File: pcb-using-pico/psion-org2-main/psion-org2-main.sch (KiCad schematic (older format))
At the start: 80 parts, among them J1 Conn_01x24_Female, J2 Conn_01x03_Female, J3 Conn_01x27_Female, J4 Conn_01x02_Female, J5 Conn_01x02_Female, J6 Conn_01x11_Female, M1 P-CH-MOSFET, M2 P-CHANNEL-MOSFET, M3 P-CHANNEL-MOSFET, U1 Pico, U10 AMS1117-3.3, U2 74HC595, U3 Regulator_Switching_MT3608, U4 74LS165, U5 74HC595, U7 MCP7940N-xSN, Y1 32k768Hz

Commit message: Updates
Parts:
- D3, D4, D5: value D -> 1N4148
- D8, D9: value D -> AECQ101
- M1: value P-CH-MOSFET -> Si2301
- M2, M3: value P-CHANNEL-MOSFET -> Si2301
- R10, R18, R24: value 110k -> 10k
- R12: value 4k7 -> 5789
- R13, R14, R15: value 100k -> 10k
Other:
- note added: "Battery measurement ciruit not tested yet\nValues unknown. Zener diode may be needed."
- note added: "JP1: leave open until output of U3 is confirmed\nat 12V."
- note added: "JP2:Leave open until ready to test the 12V\nsupply to the OLED display."
- note added: "JP4,JP6:Leave open until ready to power all of the regulators"
- note added: "Problem can occur with RTC where it holds the supply on.\nRemove R10 to disable RTC power up feature."
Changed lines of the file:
@@
 AR Path="/61545310" Ref="R12"  Part="1"
 F 0 "R12" H 10759 9621 50  0000 L CNN
-F 1 "4k7" H 10759 9530 50  0000 L CNN
+F 1 "5789" H 10759 9530 50  0000 L CNN
 F 2 "Resistor_SMD:R_0805_2012Metric" H 10700 9575 50  0001 C CNN
 F 3 "~" H 10700 9575 50  0001 C CNN
@@
 P 5625 6775
 F 0 "M1" H 5903 6821 50  0000 L CNN
-F 1 "P-CH-MOSFET" H 5903 6730 50  0000 L CNN
+F 1 "Si2301" H 5903 6730 50  0000 L CNN
 F 2 "Package_TO_SOT_SMD:SOT-23" H 5655 6925 20  0001 C CNN
 F 3 "" H 5625 6775 50  0001 C CNN
@@
 P 6825 6275
 F 0 "R14" H 6884 6321 50  0000 L CNN
-F 1 "100k" H 6884 6230 50  0000 L CNN
+F 1 "10k" H 6884 6230 50  0000 L CNN
 F 2 "Resistor_SMD:R_0805_2012Metric" H 6825 6275 50  0001 C CNN
 F 3 "~" H 6825 6275 50  0001 C CNN
@@
 P 9200 6675
 F 0 "M2" H 9478 6721 50  0000 L CNN
-F 1 "P-CHANNEL-MOSFET" H 9478 6630 50  0000 L CNN
+F 1 "Si2301" H 9478 6630 50  0000 L CNN
 F 2 "Package_TO_SOT_SMD:SOT-23" H 9230 6825 20  0001 C CNN
 F 3 "" H 9200 6675 50  0001 C CNN
@@
 P 3300 5900
 F 0 "D5" H 3300 5684 50  0000 C CNN
-F 1 "D" H 3300 5775 50  0000 C CNN
+F 1 "1N4148" H 3300 5775 50  0000 C CNN
 F 2 "Diode_SMD:D_SOD-123" H 3300 5900 50  0001 C CNN
 F 3 "~" H 3300 5900 50  0001 C CNN
@@
 P 3275 6275
 F 0 "D3" H 3275 6059 50  0000 C CNN
-F 1 "D" H 3275 6150 50  0000 C CNN
+F 1 "1N4148" H 3275 6150 50  0000 C CNN
 F 2 "Diode_SMD:D_SOD-123" H 3275 6275 50  0001 C CNN
 F 3 "~" H 3275 6275 50  0001 C CNN
@@
 P 3275 6600
 F 0 "D4" H 3275 6384 50  0000 C CNN
-F 1 "D" H 3275 6475 50  0000 C CNN
+F 1 "1N4148" H 3275 6475 50  0000 C CNN
 F 2 "Diode_SMD:D_SOD-123" H 3275 6600 50  0001 C CNN
 F 3 "~" H 3275 6600 50  0001 C CNN
@@
 P 3425 7025
 F 0 "R13" H 3484 7071 50  0000 L CNN
-F 1 "100k" H 3484 6980 50  0000 L CNN
+F 1 "10k" H 3484 6980 50  0000 L CNN
 F 2 "Resistor_SMD:R_0805_2012Metric" H 3425 7025 50  0001 C CNN
 F 3 "~" H 3425 7025 50  0001 C CNN
@@
 P 5300 6250
 F 0 "R18" H 5100 6325 50  0000 L CNN
-F 1 "110k" H 5075 6250 50  0000 L CNN
+F 1 "10k" H 5075 6250 50  0000 L CNN
 F 2 "Resistor_SMD:R_0805_2012Metric" H 5300 6250 50  0001 C CNN
 F 3 "~" H 5300 6250 50  0001 C CNN
@@
 P 5725 6250
 F 0 "R24" H 5784 6296 50  0000 L CNN
-F 1 "110k" H 5784 6205 50  0000 L CNN
+F 1 "10k" H 5784 6205 50  0000 L CNN
 F 2 "Resistor_SMD:R_0805_2012Metric" H 5725 6250 50  0001 C CNN
 F 3 "~" H 5725 6250 50  0001 C CNN
@@
 P 7650 6625
 F 0 "M3" H 7928 6671 50  0000 L CNN
-F 1 "P-CHANNEL-MOSFET" H 7928 6580 50  0000 L CNN
+F 1 "Si2301" H 7928 6580 50  0000 L CNN
 F 2 "Package_TO_SOT_SMD:SOT-23" H 7680 6775 20  0001 C CNN
 F 3 "" H 7650 6625 50  0001 C CNN
@@
 P 4900 5475
 F 0 "D8" H 4900 5259 50  0000 C CNN
-F 1 "D" H 4900 5350 50  0000 C CNN
+F 1 "AECQ101" H 4900 5350 50  0000 C CNN
 F 2 "Diode_SMD:D_SOD-123" H 4900 5475 50  0001 C CNN
 F 3 "~" H 4900 5475 50  0001 C CNN
@@
 P 5575 5475
 F 0 "D9" H 5575 5259 50  0000 C CNN
-F 1 "D" H 5575 5350 50  0000 C CNN
+F 1 "AECQ101" H 5575 5350 50  0000 C CNN
 F 2 "Diode_SMD:D_SOD-123" H 5575 5475 50  0001 C CNN
 F 3 "~" H 5575 5475 50  0001 C CNN
@@
 P 6825 6700
 F 0 "R15" H 6884 6746 50  0000 L CNN
-F 1 "100k" H 6884 6655 50  0000 L CNN
+F 1 "10k" H 6884 6655 50  0000 L CNN
 F 2 "Resistor_SMD:R_0805_2012Metric" H 6825 6700 50  0001 C CNN
 F 3 "~" H 6825 6700 50  0001 C CNN
@@
 P 4950 6475
 F 0 "R10" H 5009 6521 50  0000 L CNN
-F 1 "110k" H 5009 6430 50  0000 L CNN
+F 1 "10k" H 5009 6430 50  0000 L CNN
 F 2 "Resistor_SMD:R_0805_2012Metric" H 4950 6475 50  0001 C CNN
 F 3 "~" H 4950 6475 50  0001 C CNN
@@
 Wire Wire Line
 	8700 8350 8700 8925
+Text Notes 10800 8575 0    50   ~ 0
+JP1: leave open until output of U3 is confirmed\nat 12V.
+Text Notes 7375 8025 0    50   ~ 0
+JP2:Leave open until ready to test the 12V\nsupply to the OLED display.
+Text Notes 11200 6750 0    50   ~ 0
+JP4,JP6:Leave open until ready to power all of the regulators
+Text Notes 2475 1775 0    50   ~ 0
+Battery measurement ciruit not tested yet\nValues unknown. Zener diode may be needed.
+Text Notes 9325 1925 0    50   ~ 0
+Problem can occur with RTC where it holds the supply on.\nRemove R10 to disable RTC power up feature.
 $EndSCHEMATC

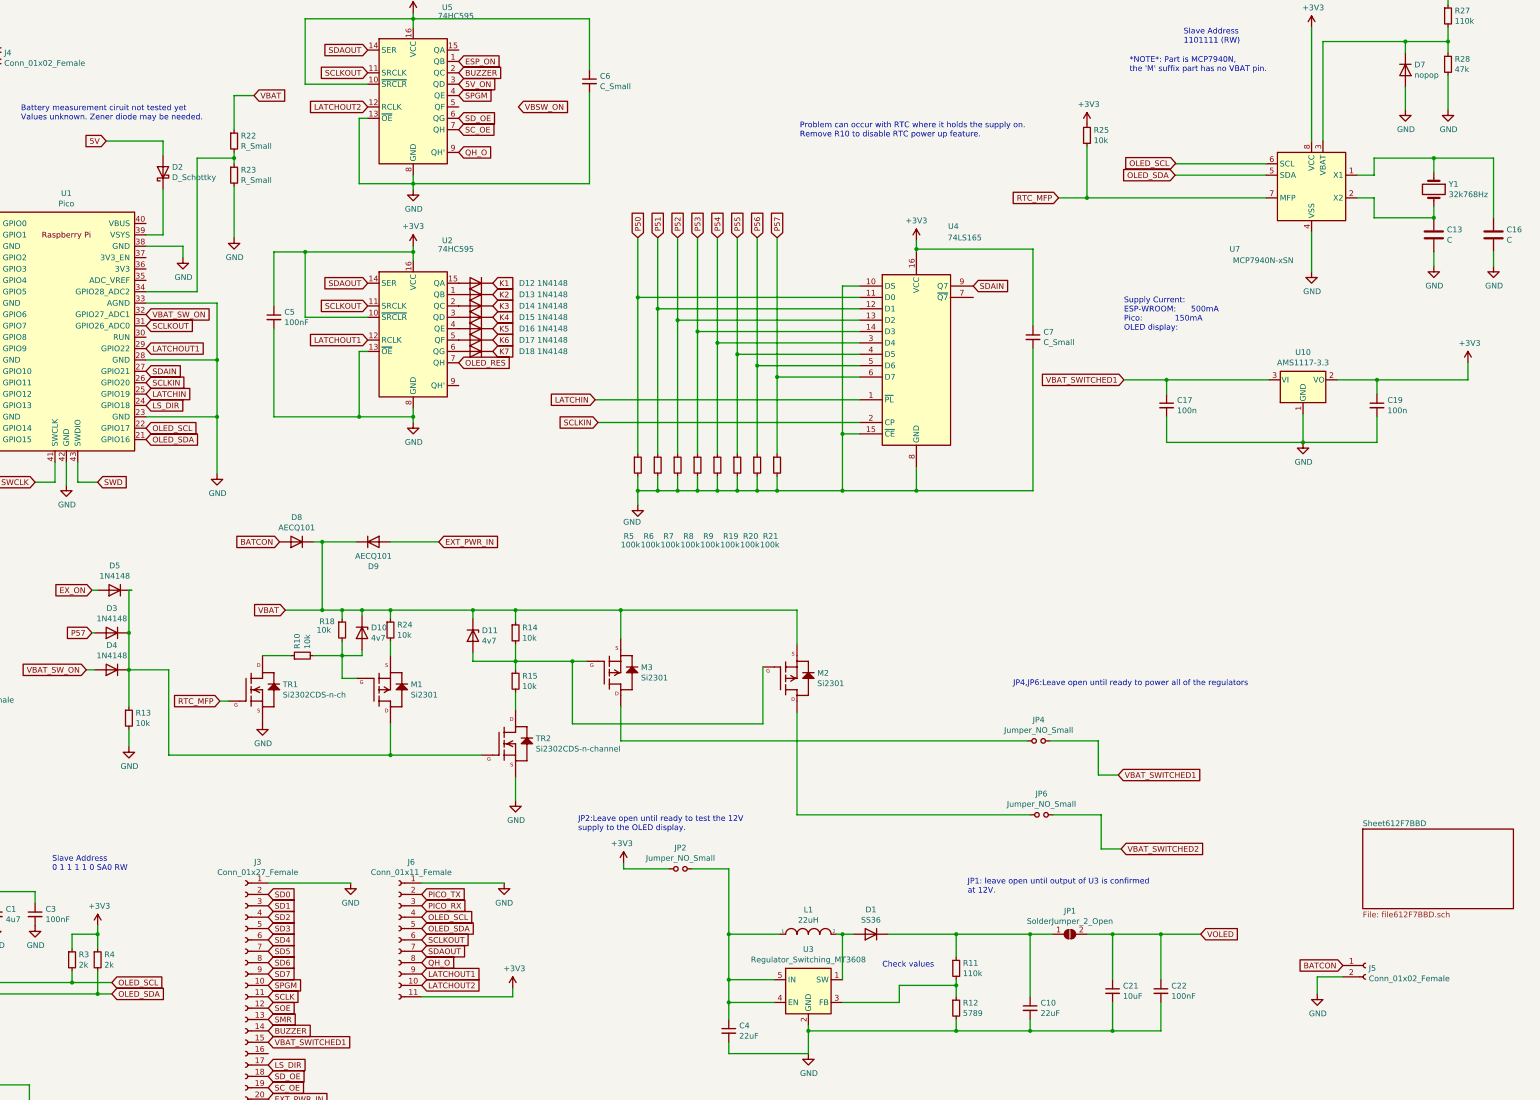
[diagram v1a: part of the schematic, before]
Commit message: Updated missing values on schematics, pushed those through to the PCB and created BOM .csv files for those schematics. Created .pdf files for schematics to mitigate the missing library problem of Kicad 5.
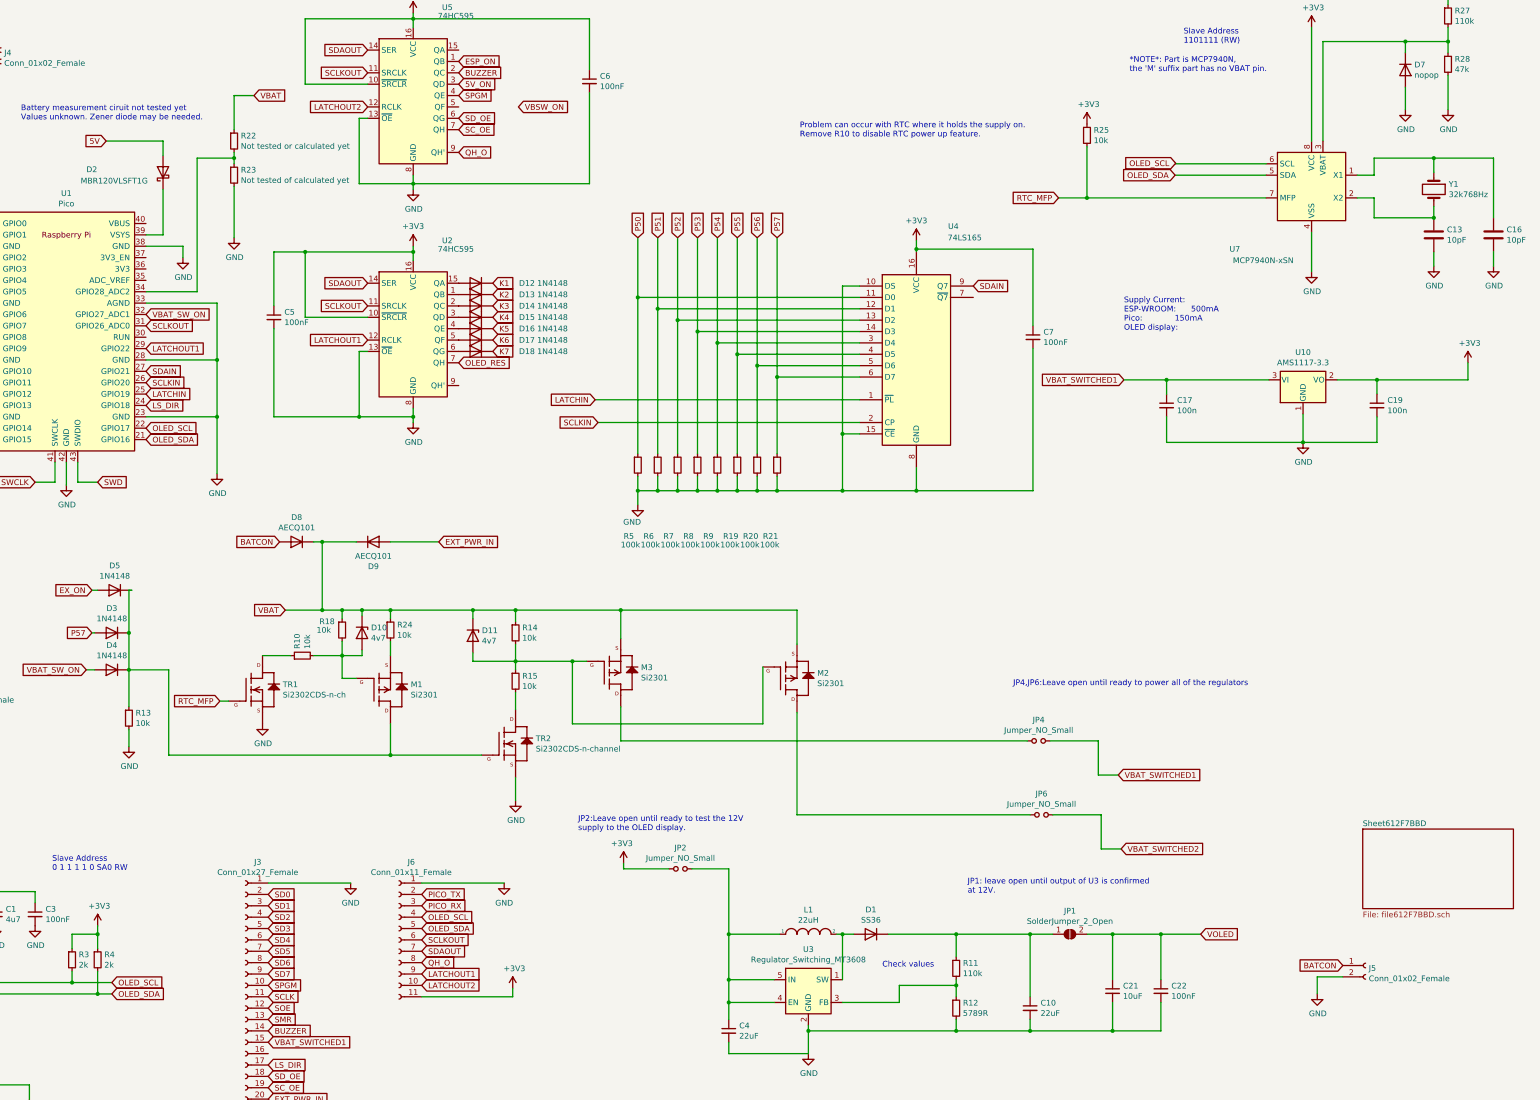
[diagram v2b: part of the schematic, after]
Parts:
- C13, C16: value C -> 10pF
- C6, C7: value C_Small -> 100nF
- D2: value D_Schottky -> MBR120VLSFT1G
- R12: value 5789 -> 5789R
- R22: value R_Small -> Not tested or calculated yet
- R23: value R_Small -> Not tested of calculated yet
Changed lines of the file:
@@
 AR Path="/61545310" Ref="R12"  Part="1"
 F 0 "R12" H 10759 9621 50  0000 L CNN
-F 1 "5789" H 10759 9530 50  0000 L CNN
+F 1 "5789R" H 10759 9530 50  0000 L CNN
 F 2 "Resistor_SMD:R_0805_2012Metric" H 10700 9575 50  0001 C CNN
 F 3 "~" H 10700 9575 50  0001 C CNN
@@
 P 4350 2250
 F 0 "R23" H 4409 2296 50  0000 L CNN
-F 1 "R_Small" H 4409 2205 50  0000 L CNN
+F 1 "Not tested of calculated yet" H 4409 2205 50  0000 L CNN
 F 2 "Resistor_SMD:R_0805_2012Metric" H 4350 2250 50  0001 C CNN
 F 3 "~" H 4350 2250 50  0001 C CNN
@@
 P 4350 1950
 F 0 "R22" H 4409 1996 50  0000 L CNN
-F 1 "R_Small" H 4409 1905 50  0000 L CNN
+F 1 "Not tested or calculated yet" H 4409 1905 50  0000 L CNN
 F 2 "Resistor_SMD:R_0805_2012Metric" H 4350 1950 50  0001 C CNN
 F 3 "~" H 4350 1950 50  0001 C CNN
@@
 U 1 1 61D07CE4
 P 3725 2225
-F 0 "D2" V 3771 2146 50  0000 R CNN
-F 1 "D_Schottky" V 3680 2146 50  0000 R CNN
+F 0 "D2" V 3750 2900 50  0000 R CNN
+F 1 "MBR120VLSFT1G" V 3650 2950 50  0000 R CNN
 F 2 "Diode_SMD:D_SOD-123" H 3725 2225 50  0001 C CNN
 F 3 "~" H 3725 2225 50  0001 C CNN
@@
 AR Path="/61F59F87" Ref="C13"  Part="1"
 F 0 "C13" H 15015 2821 50  0000 L CNN
-F 1 "C" H 15015 2730 50  0000 L CNN
+F 1 "10pF" H 15015 2730 50  0000 L CNN
 F 2 "Capacitor_SMD:C_0805_2012Metric" H 14938 2625 50  0001 C CNN
 F 3 "~" H 14900 2775 50  0001 C CNN
@@
 AR Path="/61F59F8E" Ref="C16"  Part="1"
 F 0 "C16" H 15540 2821 50  0000 L CNN
-F 1 "C" H 15540 2730 50  0000 L CNN
+F 1 "10pF" H 15540 2730 50  0000 L CNN
 F 2 "Capacitor_SMD:C_0805_2012Metric" H 15463 2625 50  0001 C CNN
 F 3 "~" H 15425 2775 50  0001 C CNN
@@
 P 11375 3675
 F 0 "C7" H 11467 3721 50  0000 L CNN
-F 1 "C_Small" H 11467 3630 50  0000 L CNN
+F 1 "100nF" H 11467 3630 50  0000 L CNN
 F 2 "Capacitor_SMD:C_0805_2012Metric" H 11375 3675 50  0001 C CNN
 F 3 "~" H 11375 3675 50  0001 C CNN
@@
 P 7475 1425
 F 0 "C6" H 7567 1471 50  0000 L CNN
-F 1 "C_Small" H 7567 1380 50  0000 L CNN
+F 1 "100nF" H 7567 1380 50  0000 L CNN
 F 2 "Capacitor_SMD:C_0805_2012Metric" H 7475 1425 50  0001 C CNN
 F 3 "~" H 7475 1425 50  0001 C CNN

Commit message: Added power board with VPP 21V supply
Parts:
- renumbered C2 to C?, C1 to C?, C3 to C?, C17 to C?, C19 to C?, C7 to C?, C6 to C?, C5 to C?, D1 to D?, D2 to D?, D12 to D?, D4 to D?, D3 to D?, D13 to D?, D14 to D?, D5 to D?, D15 to D?, D16 to D?, D17 to D?, D18 to D?, D11 to D?, D10 to D?, D8 to D?, D9 to D?, J2 to J?, J1 to J?, J5 to J?, J4 to J?, J3 to J?, J6 to J?, JP2 to JP?, JP4 to JP?, JP6 to JP?, M1 to M?, M2 to M?, M3 to M?, R1 to R?, R5 to R?, R2 to R?, R4 to R?, R3 to R?, R14 to R?, R19 to R?, R20 to R?, R21 to R?, R15 to R?, R6 to R?, R7 to R?, R8 to R?, R9 to R?, R10 to R?, R13 to R?, R23 to R?, R22 to R?, R25 to R?, R18 to R?, R24 to R?, TR2 to TR?, TR1 to TR?, U1 to U?, U2 to U?, U4 to U?, U5 to U?, U10 to U?

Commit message: Fixed comment typo. Reverted schematic to previous version (966dcfb2f9e5fb2f0f6e9c85d958500d25748731) as a change (7bf7705c572b4e37423d66cfa6dac4b195edf464) somehow managed to create a bad hierarchical page reference for the keypad. Component designations were lost and the PCB didn't update properly. I think its all fixed now, the PCB is updated and DRC runs fine.
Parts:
- gave numbers to parts that had none: 64
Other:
- note added: "Battery measurement circuit not tested yet\nValues unknown. Zener diode may be needed."
- note removed: "Battery measurement ciruit not tested yet\nValues unknown. Zener diode may be needed."

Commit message: Updates
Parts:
- added C11, C8, C9: 100nF, Capacitor_SMD:C_0805_2012Metric, symbol Device:C_Small
- added D19: nopop, Diode_SMD:D_SOD-123, symbol Device:D
- added R26: 10k, Resistor_SMD:R_0805_2012Metric, symbol Device:R_Small
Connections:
- net +3V3: no longer R25.1
- net GND: now also C8.2, D19.2 (A), R26.2
- net RTC_MFP: now also D19.1 (K), R26.1
- net VBAT: now also R25.1, C11.1, C9.1
- net at D3.1 (K), D4.1 (K), D5.1 (K)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: now also C8.1
- net at D10.2 (A), M1.1 (G), R10.2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: now also C9.2
- net at D11.2 (A), M2.1 (G), M3.1 (G)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: now also C11.2
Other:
- moved on the sheet: R10
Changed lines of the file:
@@
 Connection ~ 6825 6075
 Wire Wire Line
-	6825 6075 7750 6075
+	6825 6075 7125 6075
 Wire Wire Line
 	6825 6375 6825 6525
@@
 Connection ~ 3425 6600
 Wire Wire Line
-	3425 7125 3425 7275
+	3425 7125 3425 7225
 $Comp
 L Device:D D3
@@
 Wire Wire Line
 	13925 1075 14650 1075
-Wire Wire Line
-	13925 1075 13925 1950
 Connection ~ 14650 1075
 Wire Wire Line
-	3425 6600 3425 6925
+	3425 6600 3425 6750
 Wire Wire Line
 	3425 6600 3775 6600
@@
 U 1 1 621967D7
 P 5300 6250
-F 0 "R18" H 5100 6325 50  0000 L CNN
-F 1 "10k" H 5075 6250 50  0000 L CNN
+F 0 "R18" H 5225 6600 50  0000 L CNN
+F 1 "10k" H 5250 6525 50  0000 L CNN
 F 2 "Resistor_SMD:R_0805_2012Metric" H 5300 6250 50  0001 C CNN
 F 3 "~" H 5300 6250 50  0001 C CNN
@@
 Connection ~ 7325 6525
 Wire Wire Line
-	7325 6525 6825 6525
+	7325 6525 7125 6525
 $Comp
 L New_Library:Si2302CDS-n-channel TR1
@@
 L Device:R_Small R10
 U 1 1 61DBF060
-P 4950 6475
-F 0 "R10" H 5009 6521 50  0000 L CNN
-F 1 "10k" H 5009 6430 50  0000 L CNN
-F 2 "Resistor_SMD:R_0805_2012Metric" H 4950 6475 50  0001 C CNN
-F 3 "~" H 4950 6475 50  0001 C CNN
-	1    4950 6475
+P 4800 6475
+F 0 "R10" H 4859 6521 50  0000 L CNN
+F 1 "10k" H 4859 6430 50  0000 L CNN
+F 2 "Resistor_SMD:R_0805_2012Metric" H 4800 6475 50  0001 C CNN
+F 3 "~" H 4800 6475 50  0001 C CNN
+	1    4800 6475
 	0    -1   -1   0
 $EndComp
@@
 	5300 6075 5475 6075
 Wire Wire Line
-	5050 6475 5300 6475
+	4900 6475 5050 6475
 Connection ~ 5300 6475
 Wire Wire Line
 	5300 6475 5300 6675
 Wire Wire Line
-	4850 6475 4600 6475
+	4700 6475 4600 6475
 Wire Wire Line
 	1150 9050 1725 9050
@@
 $EndComp
 Wire Wire Line
-	13425 2450 11850 2450
+	13425 2450 12275 2450
 Wire Wire Line
 	11850 2450 11850 2000
@@
 	11850 2450 11600 2450
 Connection ~ 11850 2450
-$Comp
-L power:+3V3 #PWR?
-U 1 1 61FD52FE
-P 11850 1800
-AR Path="/61F3F57A/61FD52FE" Ref="#PWR?"  Part="1"
-AR Path="/61FD52FE" Ref="#PWR0123"  Part="1"
-F 0 "#PWR0123" H 11850 1650 50  0001 C CNN
-F 1 "+3V3" H 11865 1973 50  0000 C CNN
-F 2 "" H 11850 1800 50  0001 C CNN
-F 3 "" H 11850 1800 50  0001 C CNN
-	1    11850 1800
-	1    0    0    -1
-$EndComp
 $Comp
 L power:+3V3 #PWR?
@@
 	5125 5475 5425 5475
 Wire Wire Line
-	5125 6075 4800 6075
+	5125 6075 5050 6075
 Connection ~ 5125 6075
 $Comp
@@
 Text Notes 2475 1775 0    50   ~ 0
 Battery measurement circuit not tested yet\nValues unknown. Zener diode may be needed.
-Text Notes 9325 1925 0    50   ~ 0
+Text Notes 8450 1025 0    50   ~ 0
 Problem can occur with RTC where it holds the supply on.\nRemove R10 to disable RTC power up feature.
+$Comp
+L Device:R_Small R26
+U 1 1 6327CF0D
+P 11850 2725
+F 0 "R26" H 11909 2771 50  0000 L CNN
+F 1 "10k" H 11909 2680 50  0000 L CNN
+F 2 "Resistor_SMD:R_0805_2012Metric" H 11850 2725 50  0001 C CNN
+F 3 "~" H 11850 2725 50  0001 C CNN
+	1    11850 2725
+	1    0    0    -1
+$EndComp
+Wire Wire Line
+	13925 1075 13925 1950
+Text GLabel 11725 1300 0    50   Input ~ 0
+VBAT
+Wire Wire Line
+	11725 1300 11850 1300
+Wire Wire Line
+	11850 1300 11850 1800
+$Comp
+L power:GND #PWR0123
+U 1 1 632D7559
+P 11850 2850
+F 0 "#PWR0123" H 11850 2600 50  0001 C CNN
+F 1 "GND" H 11855 2677 50  0000 C CNN
+F 2 "" H 11850 2850 50  0001 C CNN
+F 3 "" H 11850 2850 50  0001 C CNN
+	1    11850 2850
+	1    0    0    -1
+$EndComp
+$Comp
+L Device:D D?
+U 1 1 6335213D
+P 12275 2700
+AR Path="/612F7BBE/6335213D" Ref="D?"  Part="1"
+AR Path="/6335213D" Ref="D19"  Part="1"
+F 0 "D19" V 12229 2779 50  0000 L CNN
+F 1 "nopop" V 12320 2779 50  0000 L CNN
+F 2 "Diode_SMD:D_SOD-123" H 12275 2700 50  0001 C CNN
+F 3 "~" H 12275 2700 50  0001 C CNN
+	1    12275 2700
+	0    1    1    0
+$EndComp
+Wire Wire Line
+	12275 2550 12275 2450
+Connection ~ 12275 2450
+Wire Wire Line
+	12275 2450 11850 2450
+$Comp
+L power:+3V3 #PWR0124
+U 1 1 63396013
+P 9075 2600
+F 0 "#PWR0124" H 9075 2450 50  0001 C CNN
+F 1 "+3V3" H 9090 2773 50  0000 C CNN
+F 2 "" H 9075 2600 50  0001 C CNN
+F 3 "" H 9075 2600 50  0001 C CNN
+	1    9075 2600
+	1    0    0    -1
+$EndComp
+Wire Wire Line
+	9075 2600 9075 2750
+$Comp
+L power:GND #PWR?
+U 1 1 63396042
+P 12275 2850
+AR Path="/612F7BBE/63396042" Ref="#PWR?"  Part="1"
+AR Path="/63396042" Ref="#PWR0125"  Part="1"
+F 0 "#PWR0125" H 12275 2600 50  0001 C CNN
+F 1 "GND" H 12280 2677 50  0000 C CNN
+F 2 "" H 12275 2850 50  0001 C CNN
+F 3 "" H 12275 2850 50  0001 C CNN
+	1    12275 2850
+	1    0    0    -1
+$EndComp
+Wire Wire Line
+	11850 2450 11850 2625
+Wire Wire Line
+	11850 2850 11850 2825
+$Comp
+L Device:C_Small C9
+U 1 1 6342A82D
+P 5050 6250
+F 0 "C9" H 4775 6600 50  0000 L CNN
+F 1 "100nF" H 4775 6525 50  0000 L CNN
+F 2 "Capacitor_SMD:C_0805_2012Metric" H 5050 6250 50  0001 C CNN
+F 3 "~" H 5050 6250 50  0001 C CNN
+	1    5050 6250
+	1    0    0    -1
+$EndComp
+$Comp
+L Device:C_Small C11
+U 1 1 634C7CD6
+P 7125 6275
+F 0 "C11" H 7217 6321 50  0000 L CNN
+F 1 "100nF" H 7217 6230 50  0000 L CNN
+F 2 "Capacitor_SMD:C_0805_2012Metric" H 7125 6275 50  0001 C CNN
+F 3 "~" H 7125 6275 50  0001 C CNN
+	1    7125 6275
+	1    0    0    -1
+$EndComp
+$Comp
+L Device:C_Small C8
+U 1 1 634E5F50
+P 3000 7050
+F 0 "C8" H 3092 7096 50  0000 L CNN
+F 1 "100nF" H 3092 7005 50  0000 L CNN
+F 2 "Capacitor_SMD:C_0805_2012Metric" H 3000 7050 50  0001 C CNN
+F 3 "~" H 3000 7050 50  0001 C CNN
+	1    3000 7050
+	1    0    0    -1
+$EndComp
+Wire Wire Line
+	3425 6750 3000 6750
+Wire Wire Line
+	3000 6750 3000 6950
+Connection ~ 3425 6750
+Wire Wire Line
+	3425 6750 3425 6925
+Wire Wire Line
+	3000 7150 3000 7225
+Wire Wire Line
+	3000 7225 3425 7225
+Connection ~ 3425 7225
+Wire Wire Line
+	3425 7225 3425 7275
+Wire Wire Line
+	7125 6375 7125 6525
+Connection ~ 7125 6525
+Wire Wire Line
+	7125 6525 6825 6525
+Wire Wire Line
+	7125 6175 7125 6075
+Connection ~ 7125 6075
+Wire Wire Line
+	7125 6075 7750 6075
+Wire Wire Line
+	5050 6350 5050 6475
+Connection ~ 5050 6475
+Wire Wire Line
+	5050 6475 5300 6475
+Wire Wire Line
+	5050 6150 5050 6075
+Connection ~ 5050 6075
+Wire Wire Line
+	5050 6075 4800 6075
 $EndSCHEMATC
